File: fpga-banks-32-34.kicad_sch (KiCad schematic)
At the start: 9 parts, among them U4 XC7K160T-FFG676

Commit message: [#57478] ohp release
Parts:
- C167, C168: footprint sodimm-ddr5-tester-footprints:C_0402_1005Metric -> antmicro-footprints:C_0402_1005Metric; symbol sodimm-ddr5-tester:C_100n_0402 -> antmicroCapacitors0402:C_100n_0402
- R129, R130: footprint sodimm-ddr5-tester-footprints:R_0402_1005Metric -> antmicro-footprints:R_0402_1005Metric; symbol sodimm-ddr5-tester:R_1k_0402 -> antmicroResistors0402:R_1k_0402
- R131: footprint sodimm-ddr5-tester-footprints:R_0402_1005Metric -> antmicro-footprints:R_0402_1005Metric; symbol sodimm-ddr5-tester:R_0R_0402 -> antmicroResistors0402:R_0R_0402; now not fitted; now left out of the parts list
- R132: footprint sodimm-ddr5-tester-footprints:R_0402_1005Metric -> antmicro-footprints:R_0402_1005Metric; symbol sodimm-ddr5-tester:R_0R_0402 -> antmicroResistors0402:R_0R_0402
- R133, R134: footprint sodimm-ddr5-tester-footprints:R_0402_1005Metric_EIA -> antmicro-footprints:R_0402_1005Metric_EIA; symbol sodimm-ddr5-tester:R_80R6_0402_EIA -> antmicroResistors0402:R_80R6_0402_EIA
- U4: footprint sodimm-ddr5-tester-footprints:BGA-676_27x27mm_Layout26x26_P1X1mm -> antmicro-footprints:BGA-676_27x27mm_Layout26x26_P1x1mm_FFG676; symbol sodimm-ddr5-tester:XC7K160T-FFG676 -> antmicroFPGAChips:XC7K160T-FFG676

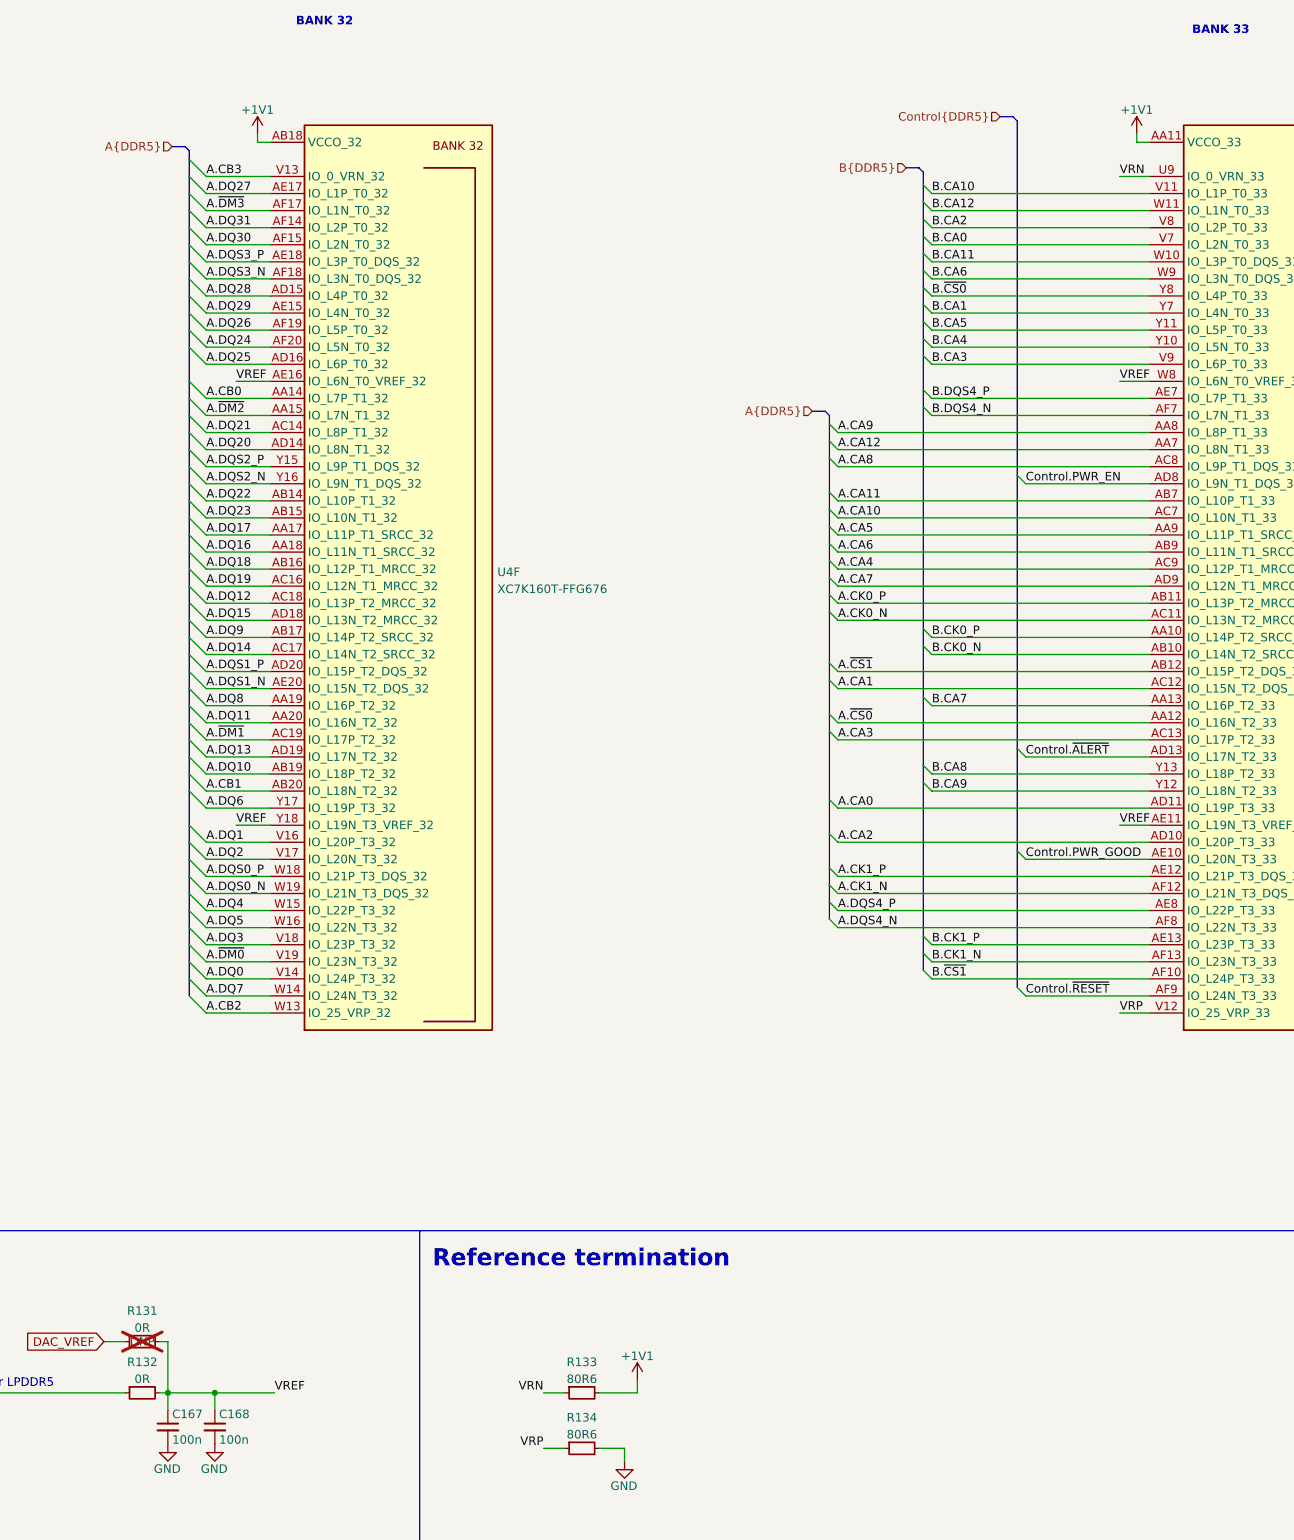
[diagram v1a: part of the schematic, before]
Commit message: [#58418] Update obsolete MPNs. Replace fuses. Remap PWR_EN and PWR_GOOD. Add UART logic level conventers. Bump revision to 1.2.0
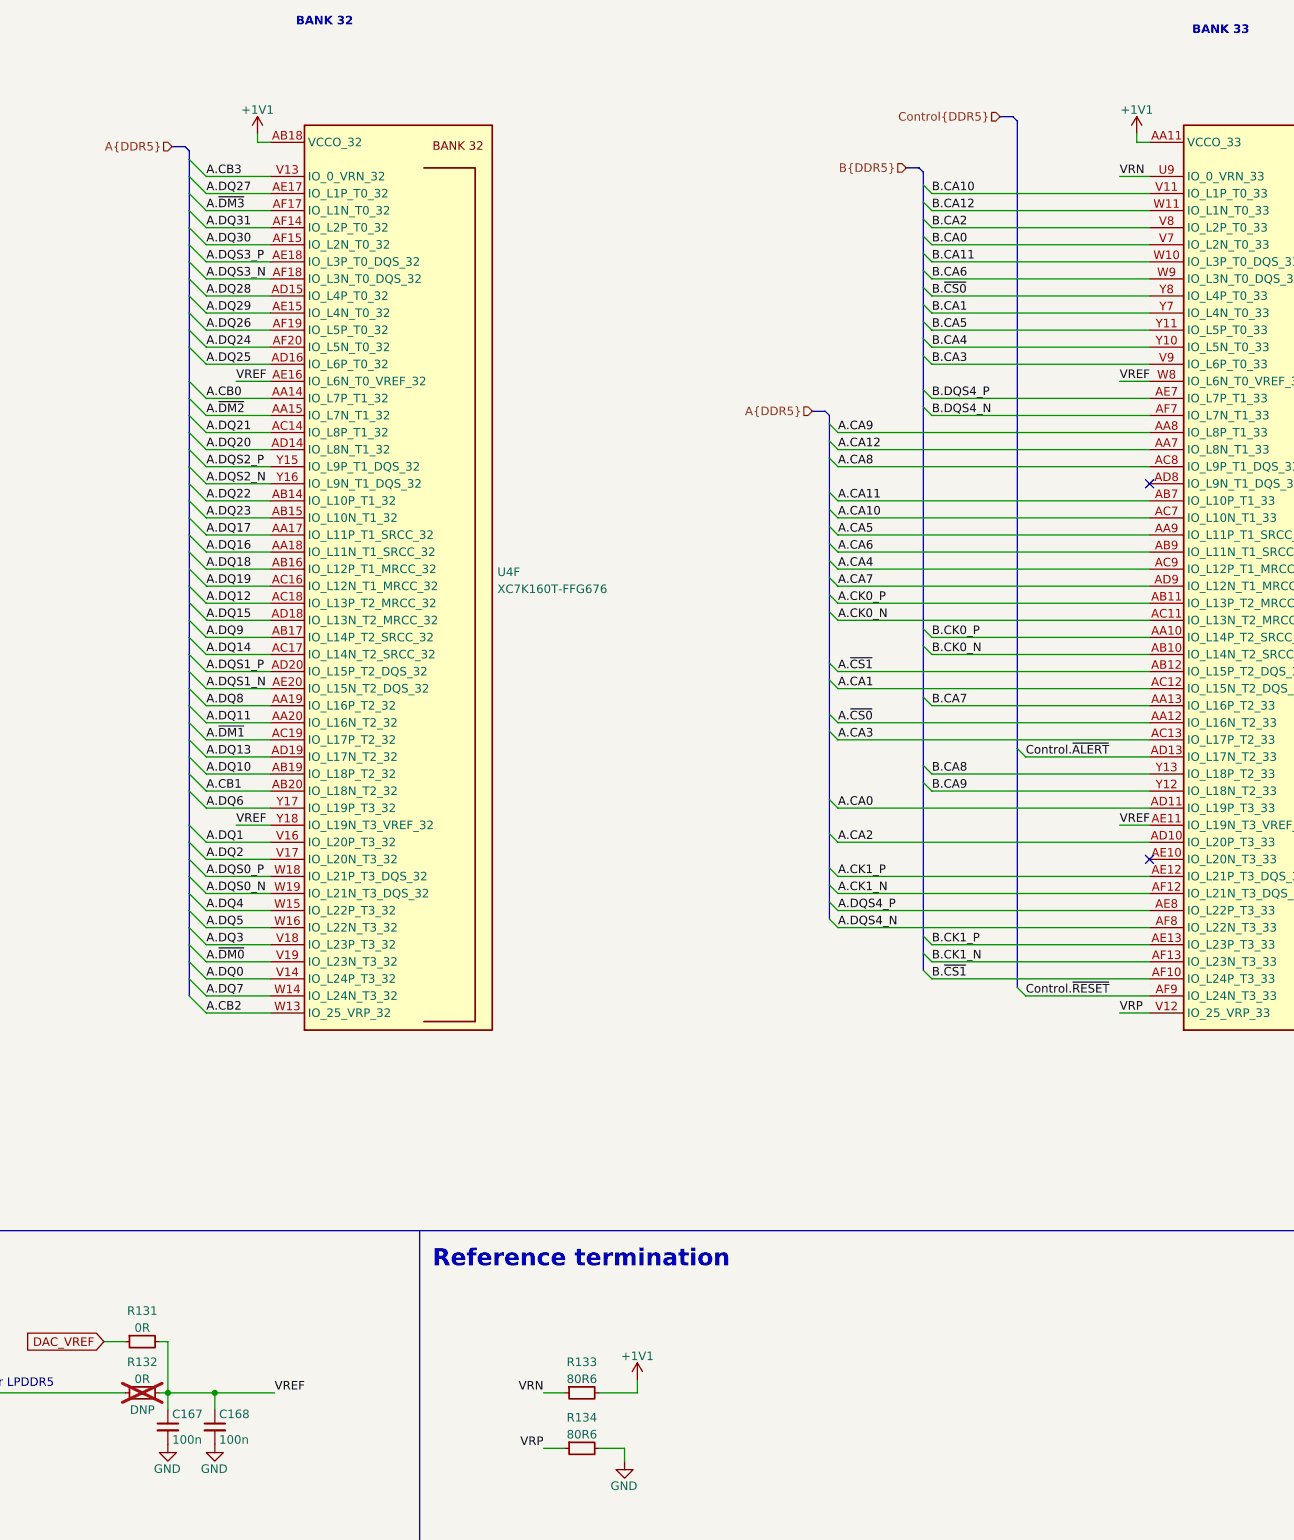
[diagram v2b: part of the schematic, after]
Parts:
- R131: DNP DNP -> (none); now fitted
- R132: DNP (none) -> DNP; now not fitted
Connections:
- net Control.PWR_EN: no longer names the net of U4.AD8 (IO_L9N_T1_DQS_33)
- net Control.PWR_GOOD: no longer names the net of U4.AE10 (IO_L20N_T3_33)
- no-connect marks 0 -> 2
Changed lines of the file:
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@@
   (title_block
     (title "SO-DIMM DDR5 Tester")
-    (date "2024-01-18")
-    (rev "1.1.1:7ba41")
+    (date "2024-04-23")
+    (rev "1.2.0")
     (company "Antmicro Ltd.")
     (comment 1 "www.antmicro.com")
@@
   (junction (at 72.39 245.745) (diameter 0) (color 0 0 0 0)
   )
+  (no_connect (at 218.44 166.37))
+  (no_connect (at 218.44 110.49))
   (bus_entry (at 78.105 115.57) (size -2.54 -2.54)
     (stroke (width 0) (type default))
@@
     (stroke (width 0) (type default))
   )
-  (bus_entry (at 198.755 165.1) (size 1.27 1.27)
-    (stroke (width 0) (type default))
-  )
   (bus_entry (at 184.785 86.36) (size 1.27 1.27)
     (stroke (width 0) (type default))
@@
     (stroke (width 0) (type default))
   )
-  (bus_entry (at 198.755 109.22) (size 1.27 1.27)
-    (stroke (width 0) (type default))
-  )
   (bus_entry (at 170.815 172.72) (size 1.27 1.27)
     (stroke (width 0) (type default))
@@
     (stroke (width 0) (type default))
   )
-  (bus (pts (xy 198.755 149.86) (xy 198.755 165.1))
-    (stroke (width 0) (type default))
-  )
   (wire (pts (xy 186.055 69.85) (xy 218.44 69.85))
     (stroke (width 0) (type default))
@@
     (stroke (width 0) (type default))
   )
-  (bus (pts (xy 198.755 56.515) (xy 198.755 109.22))
-    (stroke (width 0) (type default))
-  )
   (wire (pts (xy 72.39 245.745) (xy 79.375 245.745))
     (stroke (width 0) (type default))
@@
     (stroke (width 0) (type default))
   )
-  (bus (pts (xy 198.755 165.1) (xy 198.755 185.42))
+  (bus (pts (xy 198.755 149.86) (xy 198.755 185.42))
     (stroke (width 0) (type default))
   )
@@
     (stroke (width 0) (type default))
   )
-  (wire (pts (xy 200.025 166.37) (xy 218.44 166.37))
-    (stroke (width 0) (type default))
-  )
   (wire (pts (xy 78.105 171.45) (xy 87.63 171.45))
     (stroke (width 0) (type default))
@@
     (stroke (width 0) (type default))
   )
-  (bus (pts (xy 198.755 109.22) (xy 198.755 149.86))
+  (bus (pts (xy 198.755 56.515) (xy 198.755 149.86))
     (stroke (width 0) (type default))
   )
@@
     (stroke (width 0) (type default))
   )
-  (wire (pts (xy 200.025 110.49) (xy 218.44 110.49))
-    (stroke (width 0) (type default))
-  )
   (bus (pts (xy 304.8 135.89) (xy 304.8 138.43))
     (stroke (width 0) (type default))
@@
     (effects (font (size 1.27 1.27)) (justify left bottom))
   )
-  (label "Control.PWR_GOOD" (at 200.025 166.37 0) (fields_autoplaced)
-    (effects (font (size 1.27 1.27)) (justify left bottom))
-  )
   (label "A.CK0_P" (at 172.085 128.27 0) (fields_autoplaced)
     (effects (font (size 1.27 1.27)) (justify left bottom))
@@
     (effects (font (size 1.27 1.27)) (justify left bottom))
   )
-  (label "Control.PWR_EN" (at 200.025 110.49 0) (fields_autoplaced)
-    (effects (font (size 1.27 1.27)) (justify left bottom))
-  )
   (label "A.DQ8" (at 78.105 143.51 0) (fields_autoplaced)
     (effects (font (size 1.27 1.27)) (justify left bottom))
@@
   )
   (symbol (lib_id "antmicroResistors0402:R_0R_0402") (at 66.04 245.745 0) (unit 1)
-    (in_bom yes) (on_board yes) (dnp no) (fields_autoplaced)
+    (in_bom yes) (on_board yes) (dnp yes)
     (property "Reference" "R132" (at 68.58 241.171 0)
       (effects (font (size 1.27 1.27) (thickness 0.15)))
@@
       (effects (font (size 1.27 1.27) (thickness 0.15)) (justify left bottom) hide)
     )
+    (property "DNP" "DNP" (at 68.58 248.285 0)
+      (effects (font (size 1.27 1.27)))
+    )
     (pin "1")
     (pin "2")
@@
   )
   (symbol (lib_id "antmicroResistors0402:R_0R_0402") (at 66.04 238.125 0) (unit 1)
-    (in_bom no) (on_board yes) (dnp yes)
+    (in_bom no) (on_board yes) (dnp no)
     (property "Reference" "R131" (at 68.58 233.551 0)
       (effects (font (size 1.27 1.27) (thickness 0.15)))
@@
       (effects (font (size 1.27 1.27) (thickness 0.15)) (justify left bottom) hide)
     )
-    (property "DNP" "DNP" (at 68.58 238.125 0)
-      (effects (font (size 1.27 1.27)))
-    )
     (pin "1")

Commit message: [#86301] Project refresh 81589
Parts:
- R132: DNP DNP -> (none); now left out of the parts list
